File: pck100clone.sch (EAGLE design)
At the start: 92 parts, among them IC1 LM358N, IC3 LM358N, IC4 LM358N, IC5 LM358N, Q1 2SC945, Q2 2SC945, Q3 2N3906, Q4 2N3906, Q5 2N3904, Q6 2N3904

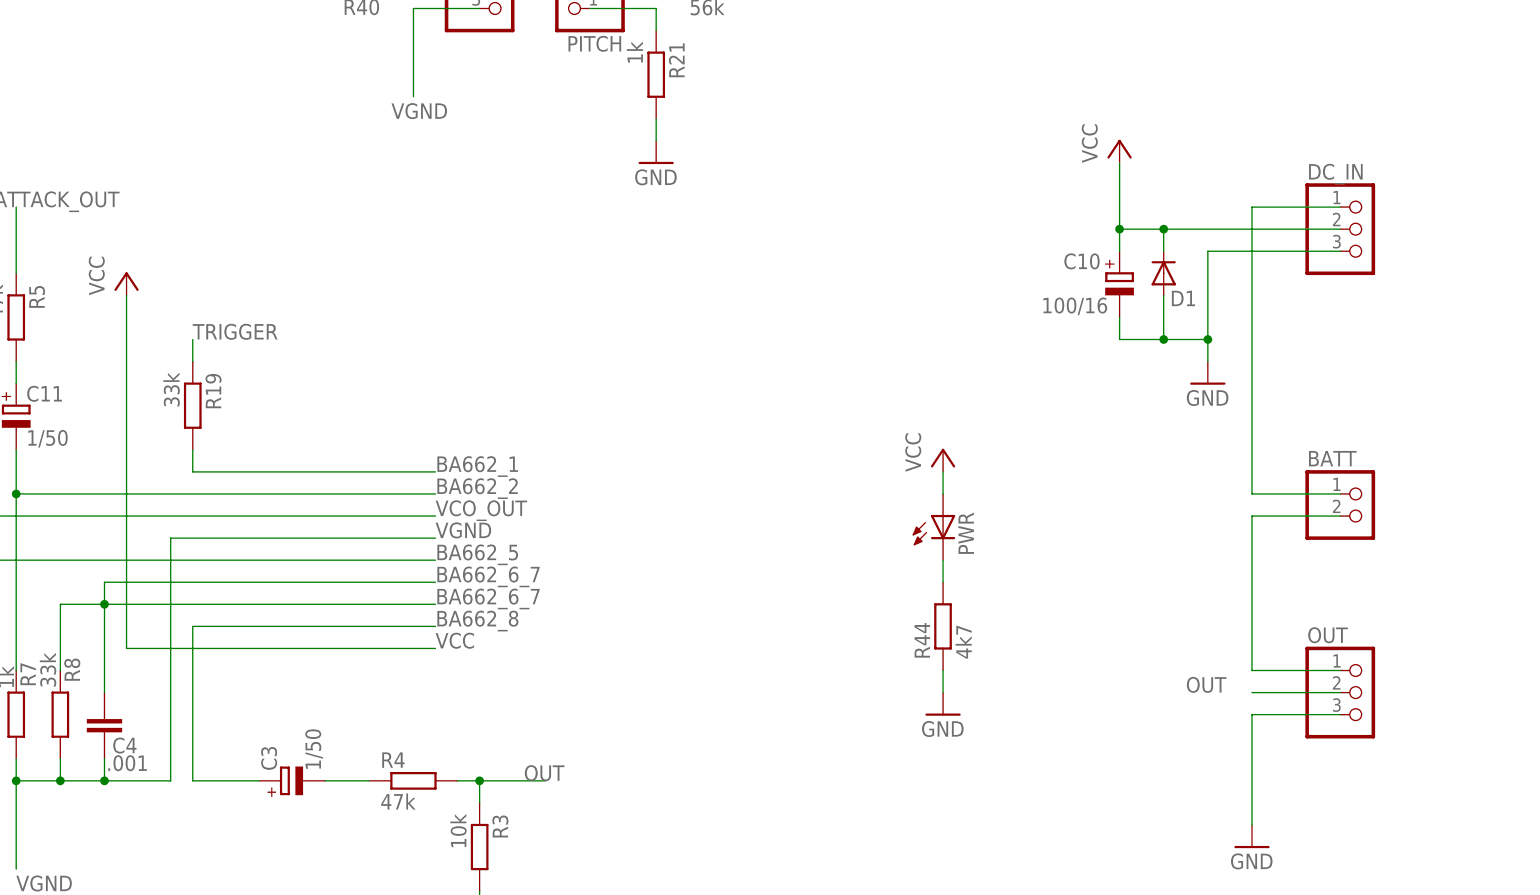
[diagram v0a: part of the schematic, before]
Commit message: added VCA pulldown
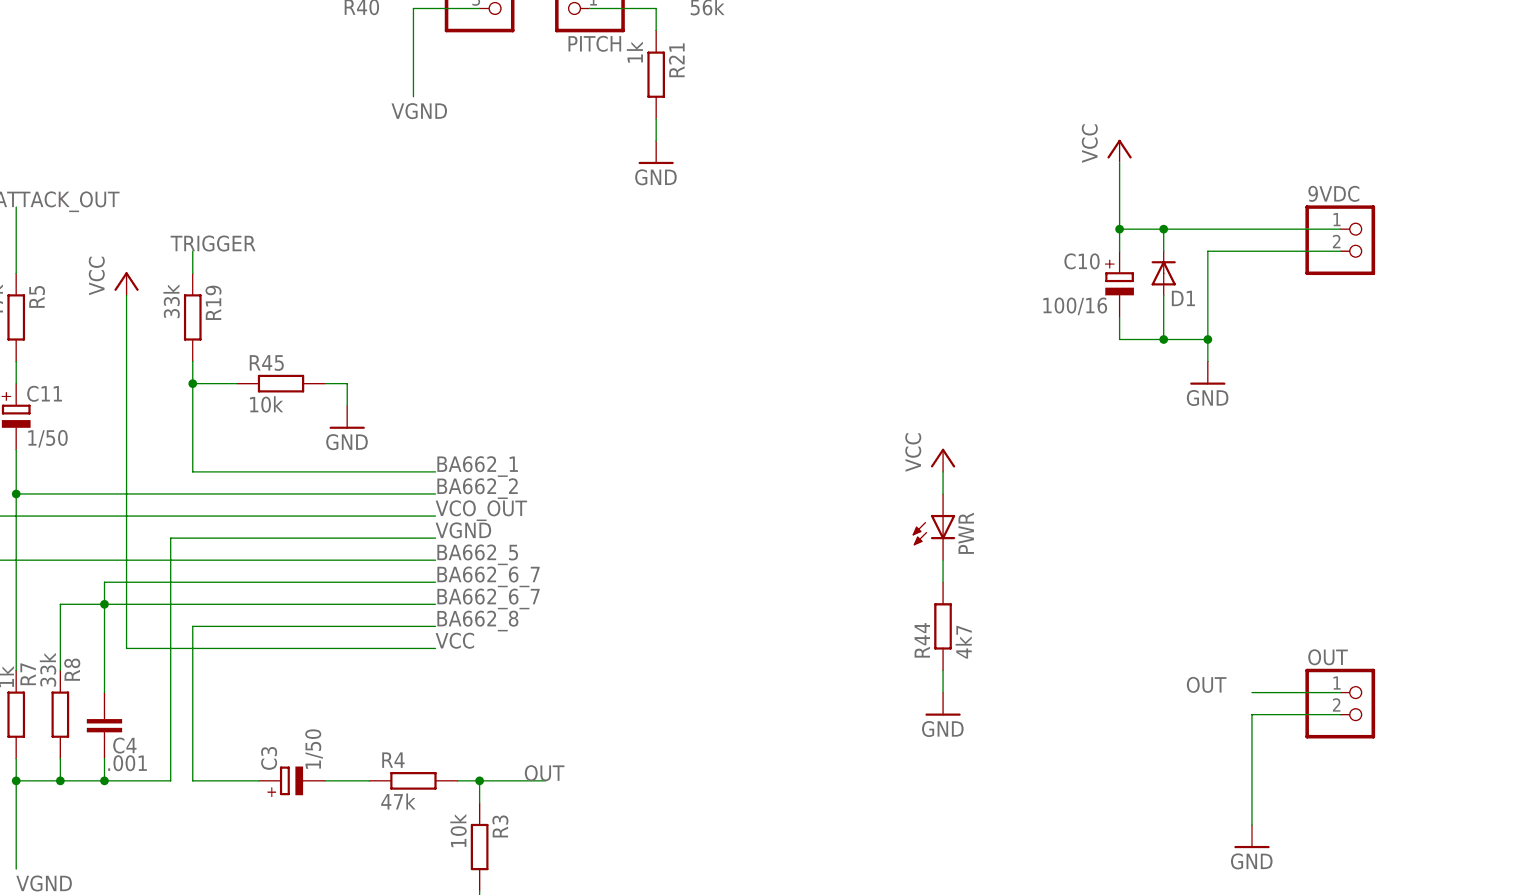
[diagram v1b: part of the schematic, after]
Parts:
- removed BATT: (no value), pinhead:PINHD-1X2
- removed DC_IN: (no value), pinhead:PINHD-1X3
- added 9VDC: (no value), pinhead:PINHD-1X2
- added R45: 10k, rcl:R-EU_0207/7
- OUT: device pinhead:PINHD-1X3 -> pinhead:PINHD-1X2
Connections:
- removed net N$50: BATT.2, OUT.1
- removed net N$54: BATT.1, DC_IN.1
- net BA662_1: now also R45.1
- net GND: now also 9VDC.2, OUT.2, R45.2; no longer DC_IN.3, OUT.3
- net OUT: now also OUT.1; no longer OUT.2
- net VCC: now also 9VDC.1; no longer DC_IN.2
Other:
- moved on the sheet: R19
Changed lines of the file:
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@@
 <part name="P+6" library="supply1" deviceset="VCC" device=""/>
 <part name="C12" library="rcl" deviceset="CPOL-EU" device="E2.5-5" value="1/50"/>
-<part name="DC_IN" library="pinhead" deviceset="PINHD-1X3" device=""/>
 <part name="C10" library="rcl" deviceset="CPOL-EU" device="E2.5-5" value="100/16"/>
 <part name="D1" library="diode" deviceset="1N4004" device=""/>
 <part name="GND23" library="supply1" deviceset="GND" device=""/>
 <part name="P+7" library="supply1" deviceset="VCC" device=""/>
-<part name="BATT" library="pinhead" deviceset="PINHD-1X2" device=""/>
 <part name="R6" library="rcl" deviceset="R-EU_" device="0207/7" value="1k"/>
 <part name="C11" library="rcl" deviceset="CPOL-EU" device="E2.5-5" value="1/50"/>
@@
 <part name="P+8" library="supply1" deviceset="VCC" device=""/>
 <part name="C3" library="rcl" deviceset="CPOL-EU" device="E2.5-5" value="1/50"/>
-<part name="OUT" library="pinhead" deviceset="PINHD-1X3" device=""/>
 <part name="R3" library="rcl" deviceset="R-EU_" device="0207/7" value="10k"/>
 <part name="R4" library="rcl" deviceset="R-EU_" device="0207/7" value="47k"/>
@@
 <part name="P+12" library="supply1" deviceset="VCC" device=""/>
 <part name="SENS_LEVEL" library="pot" deviceset="TRIM_EU-" device="CA6V"/>
+<part name="R45" library="rcl" deviceset="R-EU_" device="0207/7" value="10k"/>
+<part name="GND29" library="supply1" deviceset="GND" device=""/>
+<part name="9VDC" library="pinhead" deviceset="PINHD-1X2" device=""/>
+<part name="OUT" library="pinhead" deviceset="PINHD-1X2" device=""/>
 </parts>
 <sheets>
@@
 <instance part="P+6" gate="VCC" x="281.94" y="43.18"/>
 <instance part="C12" gate="G$1" x="317.5" y="10.16" rot="R90"/>
-<instance part="DC_IN" gate="A" x="287.02" y="-43.18"/>
 <instance part="C10" gate="G$1" x="259.08" y="-48.26" smashed="yes">
 <attribute name="NAME" x="252.603" y="-47.7774" size="1.778" layer="95"/>
@@
 <instance part="GND23" gate="1" x="269.24" y="-60.96"/>
 <instance part="P+7" gate="VCC" x="259.08" y="-33.02"/>
-<instance part="BATT" gate="G$1" x="287.02" y="-76.2"/>
 <instance part="R6" gate="G$1" x="109.22" y="-96.52" rot="R270"/>
 <instance part="C11" gate="G$1" x="132.08" y="-63.5"/>
-<instance part="R19" gate="G$1" x="152.4" y="-63.5" rot="R270"/>
+<instance part="R19" gate="G$1" x="152.4" y="-53.34" rot="R270"/>
 <instance part="R7" gate="G$1" x="132.08" y="-99.06" smashed="yes" rot="R270">
 <attribute name="NAME" x="132.5626" y="-92.964" size="1.778" layer="95" rot="R270"/>
@@
 <instance part="P+8" gate="VCC" x="144.78" y="-48.26"/>
 <instance part="C3" gate="G$1" x="162.56" y="-106.68" rot="R90"/>
-<instance part="OUT" gate="A" x="287.02" y="-96.52"/>
 <instance part="R3" gate="G$1" x="185.42" y="-114.3" rot="R270"/>
 <instance part="R4" gate="G$1" x="177.8" y="-106.68" smashed="yes">
@@
 <instance part="P+12" gate="VCC" x="109.22" y="-116.84"/>
 <instance part="SENS_LEVEL" gate="1" x="22.86" y="104.14" rot="MR270"/>
+<instance part="R45" gate="G$1" x="162.56" y="-60.96"/>
+<instance part="GND29" gate="1" x="170.18" y="-66.04"/>
+<instance part="9VDC" gate="G$1" x="287.02" y="-45.72"/>
+<instance part="OUT" gate="G$1" x="287.02" y="-99.06"/>
 </instances>
 <busses>
@@
 </segment>
 <segment>
-<pinref part="DC_IN" gate="A" pin="3"/>
 <pinref part="GND23" gate="1" pin="GND"/>
 <wire x1="284.48" y1="-45.72" x2="269.24" y2="-45.72" width="0.1524" layer="91"/>
@@
 <wire x1="259.08" y1="-55.88" x2="259.08" y2="-53.34" width="0.1524" layer="91"/>
 <junction x="264.16" y="-55.88"/>
+<pinref part="9VDC" gate="G$1" pin="2"/>
 </segment>
 <segment>
@@
 <pinref part="GND26" gate="1" pin="GND"/>
 <wire x1="274.32" y1="-99.06" x2="274.32" y2="-111.76" width="0.1524" layer="91"/>
-<pinref part="OUT" gate="A" pin="3"/>
 <wire x1="284.48" y1="-99.06" x2="274.32" y2="-99.06" width="0.1524" layer="91"/>
+<pinref part="OUT" gate="G$1" pin="2"/>
 </segment>
 <segment>
@@
 <wire x1="109.22" y1="-165.1" x2="109.22" y2="-162.56" width="0.1524" layer="91"/>
 <junction x="109.22" y="-162.56"/>
+</segment>
+<segment>
+<pinref part="R45" gate="G$1" pin="2"/>
+<pinref part="GND29" gate="1" pin="GND"/>
+<wire x1="167.64" y1="-60.96" x2="170.18" y2="-60.96" width="0.1524" layer="91"/>
+<wire x1="170.18" y1="-60.96" x2="170.18" y2="-63.5" width="0.1524" layer="91"/>
 </segment>
 </net>
@@
 <segment>
 <pinref part="R19" gate="G$1" pin="1"/>
-<wire x1="152.4" y1="-58.42" x2="152.4" y2="-55.88" width="0.1524" layer="91"/>
-<label x="152.4" y="-55.88" size="1.778" layer="95"/>
+<wire x1="152.4" y1="-48.26" x2="152.4" y2="-45.72" width="0.1524" layer="91"/>
+<label x="149.86" y="-45.72" size="1.778" layer="95"/>
 </segment>
 </net>
@@
 </segment>
 <segment>
-<pinref part="DC_IN" gate="A" pin="2"/>
 <pinref part="D1" gate="1" pin="C"/>
 <wire x1="284.48" y1="-43.18" x2="264.16" y2="-43.18" width="0.1524" layer="91"/>
@@
 <junction x="259.08" y="-43.18"/>
 <pinref part="P+7" gate="VCC" pin="VCC"/>
+<pinref part="9VDC" gate="G$1" pin="1"/>
 </segment>
 <segment>
@@
 <pinref part="R19" gate="G$1" pin="2"/>
 <wire x1="180.34" y1="-71.12" x2="152.4" y2="-71.12" width="0.1524" layer="91"/>
-<wire x1="152.4" y1="-71.12" x2="152.4" y2="-68.58" width="0.1524" layer="91"/>
+<wire x1="152.4" y1="-71.12" x2="152.4" y2="-60.96" width="0.1524" layer="91"/>
 <label x="180.34" y="-71.12" size="1.778" layer="95"/>
+<pinref part="R45" gate="G$1" pin="1"/>
+<wire x1="152.4" y1="-60.96" x2="152.4" y2="-58.42" width="0.1524" layer="91"/>
+<wire x1="157.48" y1="-60.96" x2="152.4" y2="-60.96" width="0.1524" layer="91"/>
+<junction x="152.4" y="-60.96"/>
 </segment>
 <segment>
@@
 </segment>
 </net>
-<net name="N$50" class="0">
-<segment>
-<pinref part="OUT" gate="A" pin="1"/>
-<wire x1="284.48" y1="-93.98" x2="274.32" y2="-93.98" width="0.1524" layer="91"/>
-<wire x1="274.32" y1="-93.98" x2="274.32" y2="-76.2" width="0.1524" layer="91"/>
-<pinref part="BATT" gate="G$1" pin="2"/>
-<wire x1="284.48" y1="-76.2" x2="274.32" y2="-76.2" width="0.1524" layer="91"/>
-</segment>
-</net>
 <net name="N$51" class="0">
 <segment>
@@
 </segment>
 <segment>
-<pinref part="OUT" gate="A" pin="2"/>
 <wire x1="274.32" y1="-96.52" x2="284.48" y2="-96.52" width="0.1524" layer="91"/>
 <label x="266.7" y="-96.52" size="1.778" layer="95"/>
-</segment>
-</net>
-<net name="N$54" class="0">
-<segment>
-<pinref part="DC_IN" gate="A" pin="1"/>
-<wire x1="284.48" y1="-40.64" x2="274.32" y2="-40.64" width="0.1524" layer="91"/>
-<wire x1="274.32" y1="-40.64" x2="274.32" y2="-73.66" width="0.1524" layer="91"/>
-<pinref part="BATT" gate="G$1" pin="1"/>
-<wire x1="274.32" y1="-73.66" x2="284.48" y2="-73.66" width="0.1524" layer="91"/>
-</segment>
-</net>
+<pinref part="OUT" gate="G$1" pin="1"/>
+</segment>
+</net>

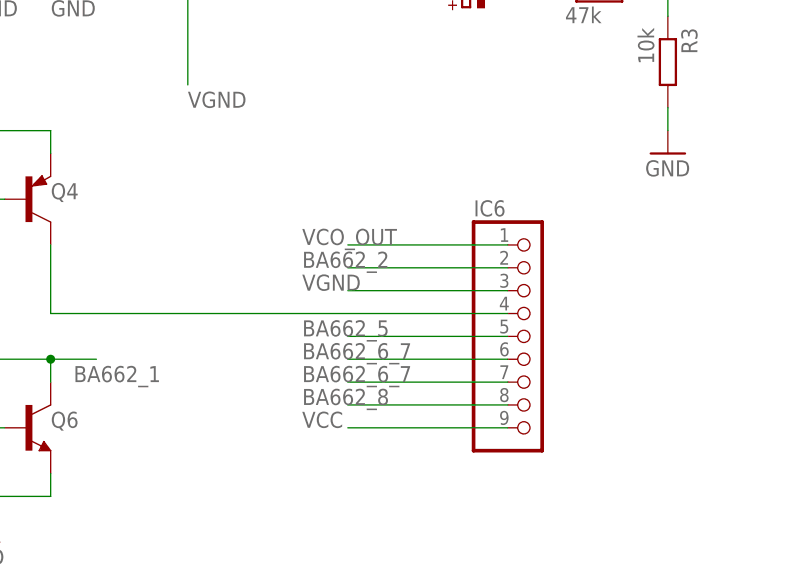
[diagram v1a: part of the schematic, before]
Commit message: remove VCA pin 3 connection to VGND
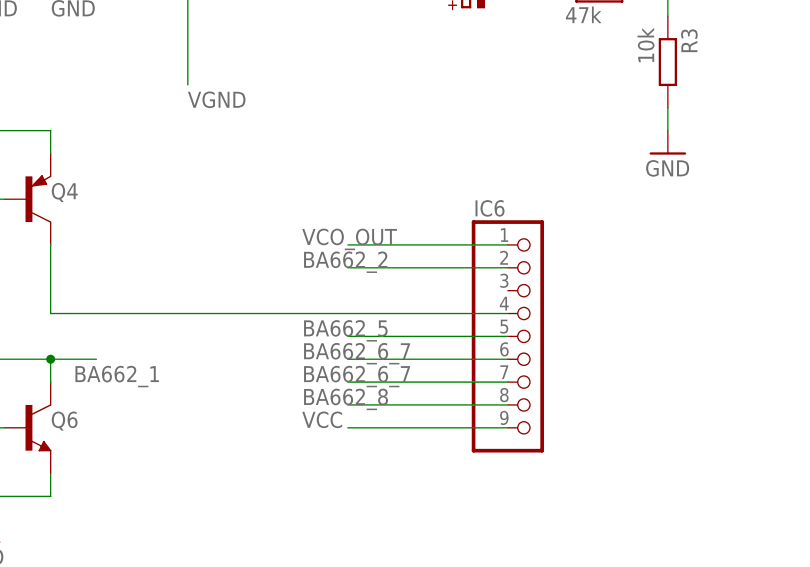
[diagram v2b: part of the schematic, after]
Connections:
- net VGND: no longer IC6.3
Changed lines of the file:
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@@
 <label x="165.1" y="-7.62" size="1.778" layer="95"/>
-</segment>
-<segment>
-<pinref part="IC6" gate="A" pin="3"/>
-<wire x1="167.64" y1="-139.7" x2="149.86" y2="-139.7" width="0.1524" layer="91"/>
-<label x="144.78" y="-139.7" size="1.778" layer="95"/>
 </segment>
 </net>

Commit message: moar stuff
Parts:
- removed ATTACK: (no value), pinhead:PINHD-1X2
- removed DIR, TRIG: (no value), pinhead:PINHD-1X3
- removed SENS_LEVEL: (no value), pot:TRIM_EU-CA6V
- added CLICK: (no value), pinhead:PINHD-1X3
- SWEEP: device pinhead:PINHD-1X3 -> pinhead:PINHD-1X4
- renumbered PIEZO to INPUT, SHAPE to SHP
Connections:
- removed net N$18: DIR.2, SWEEP.1
- removed net N$2: SENS.1, SENS_LEVEL.E, TRIG.2
- net ATTACK_OUT: now also CLICK.2; no longer ATTACK.2
- net GND: no longer SENS_LEVEL.A, TRIG.3
- net N$1: now also SENS.1; no longer TRIG.1
- net N$14: now also CLICK.1; no longer ATTACK.1
- net N$21: now also SWEEP.3; no longer SWEEP.2
- net N$24: now also SWEEP.4; no longer DIR.3
- net N$25: now also SWEEP.2; no longer DIR.1
- net N$3: no longer SENS_LEVEL.S
- net VGND: now also SWEEP.1; no longer SWEEP.3

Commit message: cv patch point
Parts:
- added JP1: (no value), pinhead:PINHD-1X1
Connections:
- net N$8: now also JP1.1
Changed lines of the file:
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@@
 <part name="SWEEP" library="pinhead" deviceset="PINHD-1X4" device=""/>
 <part name="CLICK" library="pinhead" deviceset="PINHD-1X3" device=""/>
+<part name="JP1" library="pinhead" deviceset="PINHD-1X1" device=""/>
 </parts>
 <sheets>
@@
 </instance>
 <instance part="CLICK" gate="A" x="231.14" y="99.06" rot="R90"/>
+<instance part="JP1" gate="G$1" x="83.82" y="111.76" rot="R90"/>
 </instances>
 <busses>
@@
 <wire x1="91.44" y1="86.36" x2="91.44" y2="88.9" width="0.1524" layer="91"/>
 <junction x="91.44" y="88.9"/>
-</segment>
-</net>
+<pinref part="JP1" gate="G$1" pin="1"/>
+<wire x1="83.82" y1="109.22" x2="83.82" y2="99.06" width="0.1524" layer="91"/>
+<junction x="83.82" y="99.06"/>
+</segment>
+</net>

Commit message: work in progress
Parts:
- renumbered INPUT to TRIG, MOD to DEPTH
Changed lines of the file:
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@@
 <parts>
 <part name="SENS" library="pinhead" deviceset="PINHD-1X3" device=""/>
-<part name="INPUT" library="pinhead" deviceset="PINHD-1X2" device=""/>
+<part name="TRIG" library="pinhead" deviceset="PINHD-1X2" device=""/>
 <part name="GND1" library="supply1" deviceset="GND" device=""/>
 <part name="GND3" library="supply1" deviceset="GND" device=""/>
@@
 <part name="SHP" library="pinhead" deviceset="PINHD-1X2" device=""/>
 <part name="R41" library="rcl" deviceset="R-EU_" device="0207/7" value="47k"/>
-<part name="MOD" library="pinhead" deviceset="PINHD-1X3" device=""/>
+<part name="DEPTH" library="pinhead" deviceset="PINHD-1X3" device=""/>
 <part name="PITCH" library="pinhead" deviceset="PINHD-1X3" device=""/>
 <part name="R20" library="rcl" deviceset="R-EU_" device="0207/7" value="4k7"/>
@@
 <instances>
 <instance part="SENS" gate="A" x="22.86" y="93.98" rot="R90"/>
-<instance part="INPUT" gate="G$1" x="-5.08" y="93.98" rot="R90"/>
+<instance part="TRIG" gate="G$1" x="-5.08" y="93.98" rot="R90"/>
 <instance part="GND1" gate="1" x="-7.62" y="81.28"/>
 <instance part="GND3" gate="1" x="25.4" y="81.28"/>
@@
 <instance part="SHP" gate="G$1" x="71.12" y="7.62"/>
 <instance part="R41" gate="G$1" x="55.88" y="-15.24" rot="R180"/>
-<instance part="MOD" gate="A" x="187.96" y="-15.24"/>
+<instance part="DEPTH" gate="A" x="187.96" y="-15.24"/>
 <instance part="PITCH" gate="A" x="195.58" y="-15.24" rot="R180"/>
 <instance part="R20" gate="G$1" x="154.94" y="10.16" rot="R180"/>
@@
 <net name="GND" class="0">
 <segment>
-<pinref part="INPUT" gate="G$1" pin="1"/>
+<pinref part="TRIG" gate="G$1" pin="1"/>
 <pinref part="GND1" gate="1" pin="GND"/>
 <wire x1="-7.62" y1="91.44" x2="-7.62" y2="83.82" width="0.1524" layer="91"/>
@@
 <net name="N$1" class="0">
 <segment>
-<pinref part="INPUT" gate="G$1" pin="2"/>
+<pinref part="TRIG" gate="G$1" pin="2"/>
 <wire x1="-5.08" y1="91.44" x2="-5.08" y2="86.36" width="0.1524" layer="91"/>
 <wire x1="-5.08" y1="86.36" x2="20.32" y2="86.36" width="0.1524" layer="91"/>
@@
 </segment>
 <segment>
-<pinref part="MOD" gate="A" pin="3"/>
+<pinref part="DEPTH" gate="A" pin="3"/>
 <wire x1="185.42" y1="-17.78" x2="177.8" y2="-17.78" width="0.1524" layer="91"/>
 <wire x1="177.8" y1="-17.78" x2="177.8" y2="-27.94" width="0.1524" layer="91"/>
@@
 <pinref part="IC4" gate="B" pin="+IN"/>
 <wire x1="185.42" y1="20.32" x2="193.04" y2="20.32" width="0.1524" layer="91"/>
-<pinref part="MOD" gate="A" pin="1"/>
+<pinref part="DEPTH" gate="A" pin="1"/>
 <wire x1="193.04" y1="20.32" x2="195.58" y2="20.32" width="0.1524" layer="91"/>
 <wire x1="185.42" y1="-12.7" x2="177.8" y2="-12.7" width="0.1524" layer="91"/>
@@
 <segment>
 <pinref part="R40" gate="G$1" pin="1"/>
-<pinref part="MOD" gate="A" pin="2"/>
+<pinref part="DEPTH" gate="A" pin="2"/>
 <wire x1="175.26" y1="-15.24" x2="185.42" y2="-15.24" width="0.1524" layer="91"/>
 </segment>

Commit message: rev2
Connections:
- net GND: now also CLICK.3
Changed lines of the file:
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@@
 <part name="CLICK" library="pinhead" deviceset="PINHD-1X3" device=""/>
 <part name="JP1" library="pinhead" deviceset="PINHD-1X1" device=""/>
+<part name="GND2" library="supply1" deviceset="GND" device=""/>
 </parts>
 <sheets>
@@
 <instance part="CLICK" gate="A" x="231.14" y="99.06" rot="R90"/>
 <instance part="JP1" gate="G$1" x="83.82" y="111.76" rot="R90"/>
+<instance part="GND2" gate="1" x="233.68" y="78.74"/>
 </instances>
 <busses>
@@
 <wire x1="170.18" y1="-60.96" x2="170.18" y2="-63.5" width="0.1524" layer="91"/>
 </segment>
+<segment>
+<pinref part="CLICK" gate="A" pin="3"/>
+<wire x1="233.68" y1="96.52" x2="233.68" y2="81.28" width="0.1524" layer="91"/>
+<pinref part="GND2" gate="1" pin="GND"/>
+</segment>
 </net>

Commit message: rev3
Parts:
- added JP100, JP101, JP102, JP103, JP104, JP105, JP106, JP107, JP108, JP109, JP110, JP111, JP112, JP113, JP114, JP115, JP116, JP117, JP118, JP119, JP120, JP121, JP122, JP123, JP124, JP125, JP126, JP127, JP128, JP129, JP130, JP131, JP132, JP133, JP134, JP135, JP136, JP14, JP143, JP144, JP145, JP15, JP16, JP17, JP18, JP19, JP2, JP20, JP21, JP22, JP23, JP24, JP25, JP26, JP27, JP28, JP29, JP3, JP30, JP31, JP32, JP33, JP34, JP35, JP36, JP37, JP38, JP39, JP4, JP40, JP41, JP42, JP43, JP44, JP45, JP46, JP47, JP48, JP49, JP5, JP50, JP51, JP52, JP53, JP54, JP55, JP56, JP57, JP58, JP59, JP6, JP60, JP61, JP62, JP63, JP64, JP65, JP66, JP67, JP68, JP69, JP7, JP70, JP71, JP72, JP73, JP74, JP75, JP76, JP77, JP78, JP79, JP80, JP81, JP82, JP83, JP84, JP85, JP86, JP87, JP88, JP89, JP90, JP91, JP92, JP93, JP94, JP95, JP96, JP97, JP98, JP99: (no value), pinhead:PINHD-1X1
- R45: value 10k -> 4k7
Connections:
- new net N$100: JP120.1, JP122.1, JP123.1
- new net N$101: JP124.1, JP125.1, JP126.1
- new net N$102: JP127.1, JP128.1, JP132.1
- new net N$103: JP129.1, JP130.1, JP131.1
- new net N$104: JP133.1, JP134.1, JP135.1
- new net N$18: JP4.1, JP5.1, JP6.1
- new net N$50: JP14.1, JP15.1, JP19.1
- new net N$52: JP16.1, JP17.1, JP18.1
- new net N$53: JP20.1, JP21.1, JP25.1
- new net N$54: JP22.1, JP23.1, JP24.1
- new net N$55: JP26.1, JP27.1, JP31.1
- new net N$56: JP28.1, JP29.1, JP30.1
- new net N$57: JP32.1, JP33.1, JP34.1
- new net N$58: JP35.1, JP36.1, JP37.1
- new net N$59: JP38.1, JP39.1, JP40.1
- new net N$60: JP41.1, JP42.1, JP43.1
- new net N$64: JP53.1, JP54.1, JP55.1
- new net N$65: JP56.1, JP57.1, JP61.1
- new net N$67: JP62.1, JP63.1, JP67.1
- new net N$68: JP64.1, JP65.1, JP66.1
- new net N$69: JP68.1, JP69.1, JP73.1
- new net N$70: JP70.1, JP71.1, JP72.1
- new net N$71: JP74.1, JP75.1, JP76.1
- new net N$72: JP77.1, JP78.1, JP79.1
- new net N$73: JP136.1, JP80.1, JP81.1
- new net N$89: JP105.1, JP98.1, JP99.1
- new net N$90: JP82.1, JP83.1, JP89.1
- new net N$91: JP85.1, JP86.1, JP87.1
- new net N$92: JP101.1, JP102.1, JP103.1
- new net N$93: JP106.1, JP107.1, JP113.1
- new net N$94: JP109.1, JP110.1, JP111.1
- new net N$95: JP114.1, JP115.1, JP121.1
- new net N$96: JP117.1, JP118.1, JP119.1
- new net N$97: JP84.1, JP88.1, JP92.1
- new net N$98: JP100.1, JP104.1, JP96.1
- new net N$99: JP108.1, JP112.1, JP116.1
- net GND: now also JP47.1, JP48.1, JP49.1, JP50.1, JP51.1, JP52.1, JP90.1, JP91.1, JP93.1, JP94.1, JP95.1, JP97.1
- net VCC: now also JP143.1, JP144.1, JP145.1, JP2.1, JP3.1, JP44.1, JP45.1, JP46.1, JP58.1, JP59.1, JP60.1, JP7.1
